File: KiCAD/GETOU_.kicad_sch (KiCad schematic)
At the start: 25 parts, among them U1 XIAO-RP2040-DIP

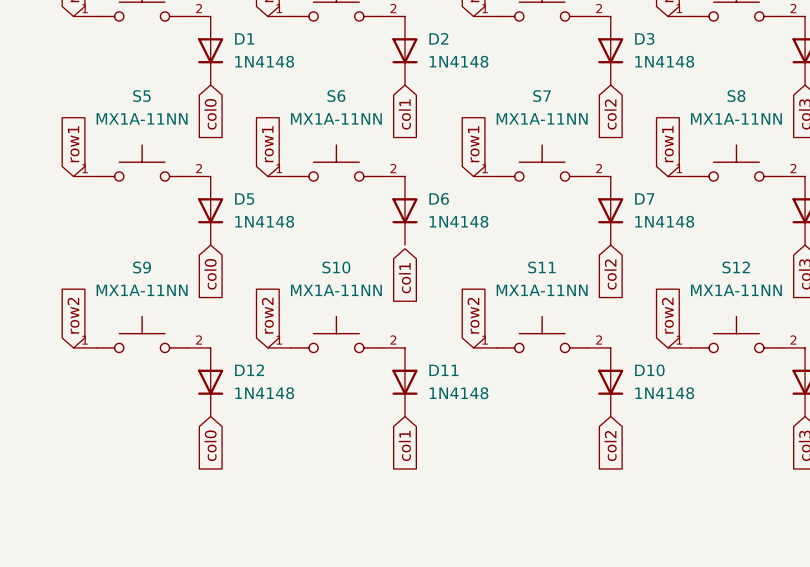
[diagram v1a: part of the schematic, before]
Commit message: Fix values in GETOU_ project files for improved accuracy
- Updated numerical values in GETOU_.kicad_prl to correct component specifications.
- Adjusted positions of global labels in GETOU_.kicad_sch for better alignment and clarity.
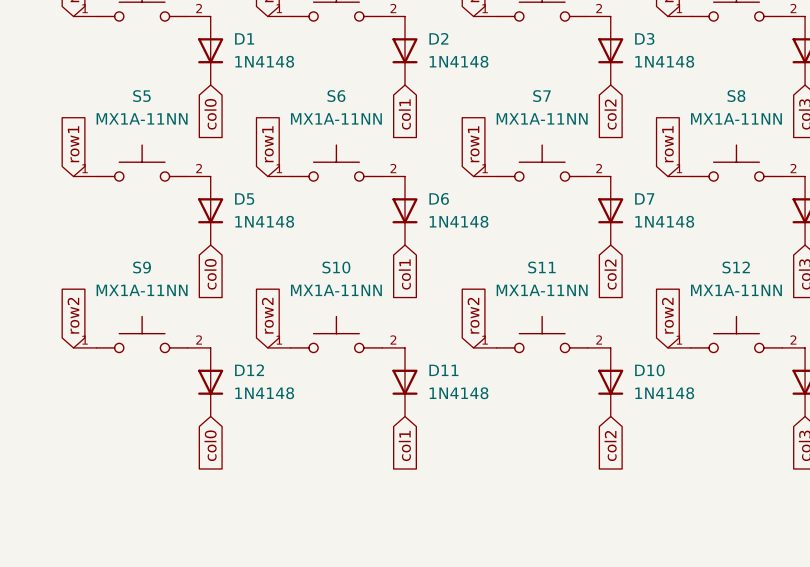
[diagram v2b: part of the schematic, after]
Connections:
- net col1: now also D6.1 (K)
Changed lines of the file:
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@@
 	(global_label "col1"
 		(shape input)
-		(at 106.68 84.2302 270)
+		(at 106.68 83.82 270)
 		(fields_autoplaced yes)
 		(effects
@@
 		)
 		(property "Intersheetrefs" "${INTERSHEET_REFS}"
-			(at 106.68 91.3277 90)
+			(at 106.68 90.9175 90)
 			(hide yes)
 			(show_name no)

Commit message: Modify Files
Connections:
- net col0: now also D11.1 (K), D4.1 (K), D7.1 (K); no longer D12.1 (K), D5.1 (K)
- net col1: now also D10.1 (K), D5.1 (K), D8.1 (K); no longer D11.1 (K), D6.1 (K)
- net col2: now also D12.1 (K), D6.1 (K), D9.1 (K); no longer D10.1 (K), D7.1 (K)
- net row0: no longer S4.1
- net row1: now also S4.1; no longer S7.1, S8.1
- net row2: now also S7.1, S8.1; no longer S10.1, S11.1, S12.1
- removed net col3: D4.1 (K), D8.1 (K), D9.1 (K), U1.6 (GPIO7/SCL)
- new net row3: S10.1, S11.1, S12.1, U1.6 (GPIO7/SCL)
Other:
- moved on the sheet: D10, D11, D12, D4, D5, D6, D7, D8, D9, S10, S11, S12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
